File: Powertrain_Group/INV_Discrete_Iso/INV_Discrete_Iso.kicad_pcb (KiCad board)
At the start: 4 copper layers, 100 x 40.5 mm, 69 parts, among them IC1 UCC33420QRAQRQ1, IC2 UCC33420QRAQRQ1, IC4 UCC33420QRAQRQ1, J1 Conn_01x04_Socket, J10 15130122601000, J2 Conn_01x04_Socket, J3 Conn_01x04_Socket, J4 Conn_01x04_Socket, J5 Conn_01x04_Socket, J6 Conn_01x04_Socket, J7 Conn_01x04_Socket, J8 Conn_01x04_Socket, J9 Conn_01x04_Socket, U1 MGJ2D241802SC, U2 MGJ2D241802SC, U3 ISO7720DWV, U4 MGJ2D241802SC, U5 MGJ2D241802SC, U6 ISO7720DWV, U7 MGJ2D241802SC, U8 MGJ2D241802SC, U9 ISO7720DWV

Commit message: [INV_Discrete_Iso] V1.1
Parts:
- IC1, IC2, IC4: footprint nturt_kicad_lib_EP6:UCC33020QRAQRQ1 -> nturt_kicad_lib_EP7:UCC33020
- J1: value Conn_01x04_Socket -> U_ISOPWR_H
- J10: value 15130122601000 -> Harting 15130122601000; footprint nturt_kicad_lib_EP6:15130122601000 -> nturt_kicad_lib_EP7:Harting_15130122601000
- J2: value Conn_01x04_Socket -> U_PWM
- J3: value Conn_01x04_Socket -> U_ISOPWR_L
- J4: value Conn_01x04_Socket -> V_ISOPWR_H
- J5: value Conn_01x04_Socket -> V_PWM
- J6, J9: value Conn_01x04_Socket -> W_ISOPWR_L
- J7: value Conn_01x04_Socket -> W_ISOPWR_H
- J8: value Conn_01x04_Socket -> W_PWM
- R1: value 1K -> 10k
- R7: value 10k -> 22k
- moved D2 1.54 mm to (131.1, 71.3)
- moved C5 0.40 mm to (151.6, 72.4)
- moved C39 0.40 mm to (186.7, 72.3)
- moved R1 0.40 mm to (138.2, 70.4)
- moved C29 0.26 mm to (116.8, 70.6)
- moved C25 0.25 mm to (116.8, 72.4)
- moved C9 0.12 mm to (151.5, 70.6)
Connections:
- net /iso_half_bridge_U/+V_H renamed /iso_half_bridge_U/ISO_18V_H
- net /iso_half_bridge_U/+V_L renamed /iso_half_bridge_U/ISO_18V_L
- net /iso_half_bridge_U/-V_H renamed /iso_half_bridge_U/ISO_2.5V_H
- net /iso_half_bridge_U/-V_L renamed /iso_half_bridge_U/ISO_2.5V_L
- net /iso_half_bridge_U/GND_H renamed /iso_half_bridge_U/ISO_GND_H
- net /iso_half_bridge_U/GND_L renamed /iso_half_bridge_U/ISO_GND_L
- net /iso_half_bridge_U/iso_5V renamed /iso_half_bridge_U/ISO_5V
- net /iso_half_bridge_U/iso_GND renamed /iso_half_bridge_U/ISO_GND
- net /iso_half_bridge_V/+V_H renamed /iso_half_bridge_V/ISO_18V_H
- net /iso_half_bridge_V/+V_L renamed /iso_half_bridge_V/ISO_18V_L
- net /iso_half_bridge_V/-V_H renamed /iso_half_bridge_V/ISO_2.5V_H
- net /iso_half_bridge_V/-V_L renamed /iso_half_bridge_V/ISO_2.5V_L
- net /iso_half_bridge_V/GND_H renamed /iso_half_bridge_V/ISO_GND_H
- net /iso_half_bridge_V/GND_L renamed /iso_half_bridge_V/ISO_GND_L
- net /iso_half_bridge_V/iso_5V renamed /iso_half_bridge_V/ISO_5V
- net /iso_half_bridge_V/iso_GND renamed /iso_half_bridge_V/ISO_GND
- net /iso_half_bridge_W/+V_H renamed /iso_half_bridge_W/ISO_18V_H
- net /iso_half_bridge_W/+V_L renamed /iso_half_bridge_W/ISO_18V_L
- net /iso_half_bridge_W/-V_H renamed /iso_half_bridge_W/ISO_2.5V_H
- net /iso_half_bridge_W/-V_L renamed /iso_half_bridge_W/ISO_2.5V_L
- net /iso_half_bridge_W/GND_H renamed /iso_half_bridge_W/ISO_GND_H
- net /iso_half_bridge_W/GND_L renamed /iso_half_bridge_W/ISO_GND_L
- net /iso_half_bridge_W/iso_5V renamed /iso_half_bridge_W/ISO_5V
- net /iso_half_bridge_W/iso_GND renamed /iso_half_bridge_W/ISO_GND
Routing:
- net +3.3V: track 99.5 -> 104.1 mm
- net /U_PWM+: track 27.4 -> 24.8 mm, vias 3 -> 2
- net /W_PWM+: track 99.0 -> 96.7 mm
- net /W_PWM-: track 99.3 -> 97.0 mm
- net /V_PWM+: track 52.8 -> 51.0 mm, vias 3 -> 2
- net /V_PWM-: track 54.9 -> 53.3 mm, vias 3 -> 2
- net Net-(D2-K): track 1.61 -> 0.70 mm
- net /U_PWM-: track 30.2 -> 29.4 mm, vias 3 -> 2
- net +24V: track 12.2 -> 12.4 mm, vias 1 -> 3
- net +5V: track 98.0 -> 97.8 mm, vias 8 -> 7
- net GND: vias 132 -> 149
- removed copper zone on In2.Cu, net +5V
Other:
- board text added: "+24V"
- board text added: "+5V"
- board text added: "EP7 INV_Discrete_Iso V1.1 2026/03/14 LY Chen, Jack Kuo"
- board text removed: "INV ISO Board_V1.0 2026/02/20 LY Chen"

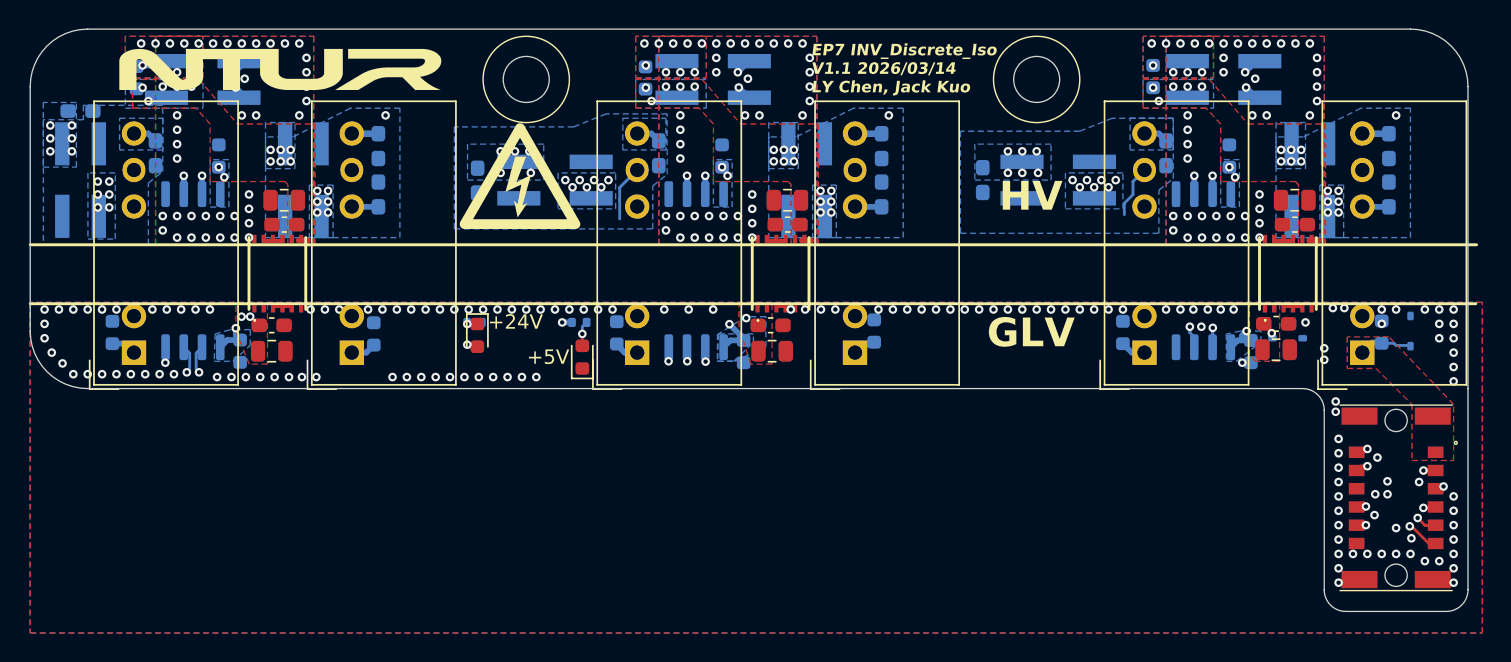
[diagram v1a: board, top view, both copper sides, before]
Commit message: [INV_Discrete_Iso] V1.2
fix connector to controller board mismatch
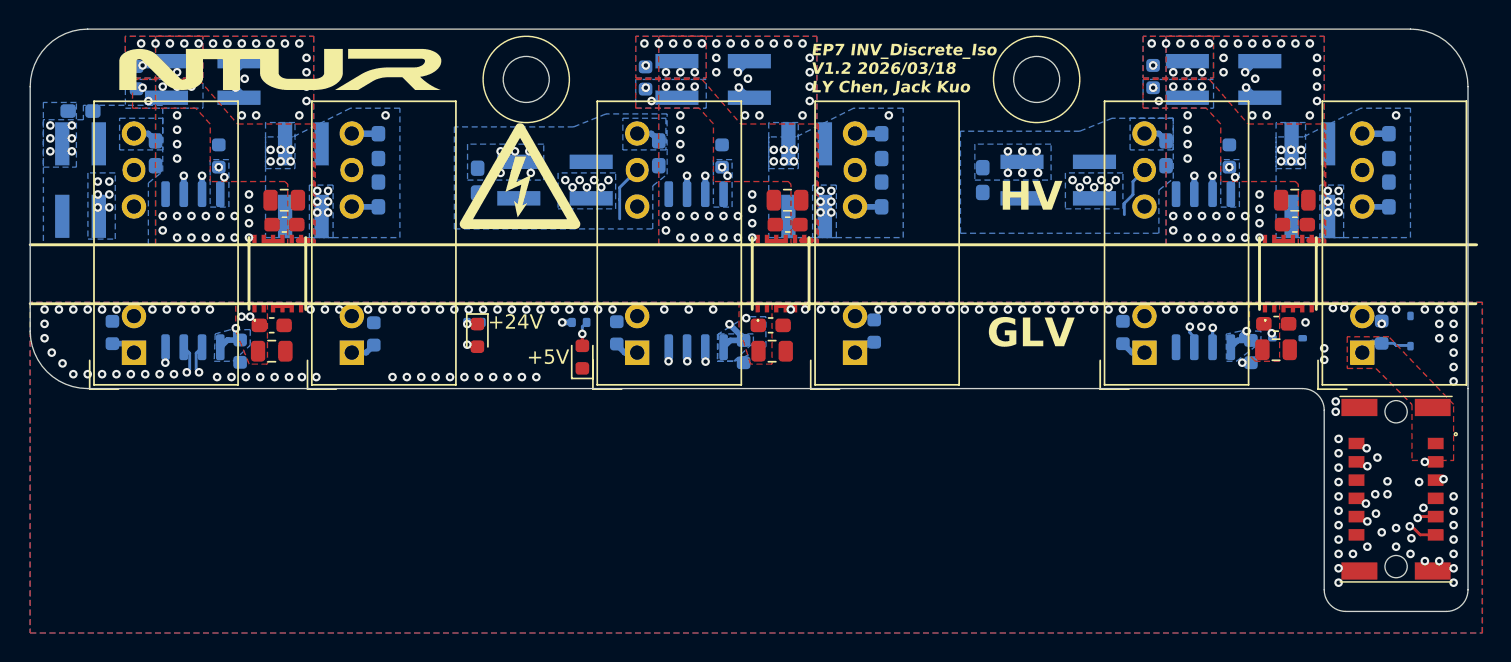
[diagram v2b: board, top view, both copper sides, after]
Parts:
- J6: value W_ISOPWR_L -> V_ISOPWR_L
- moved J10 0.60 mm to (195.0, 82.0)
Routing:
- net /U_PWM+: track 24.8 -> 23.9 mm
- net /U_PWM-: track 29.4 -> 28.6 mm
- net +3.3V: track 104.1 -> 103.4 mm
- net +5V: track 97.8 -> 97.3 mm
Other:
- board text added: "EP7 INV_Discrete_Iso V1.2 2026/03/18 LY Chen, Jack Kuo"
- board text removed: "EP7 INV_Discrete_Iso V1.1 2026/03/14 LY Chen, Jack Kuo"
